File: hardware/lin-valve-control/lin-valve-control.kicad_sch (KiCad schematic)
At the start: 27 parts, among them J1 QWIIC Connector, J2 DIN-5_180degree, J3 DIN-5_180degree, J4 Screw_Terminal_01x02, J5 Screw_Terminal_01x03, J6 Screw_Terminal_01x03, Q1 2N7002, Q2 2N7002, U1 Arduino_Nano_v3.x, U2 TJA1021T, U3 DRV8833PWP

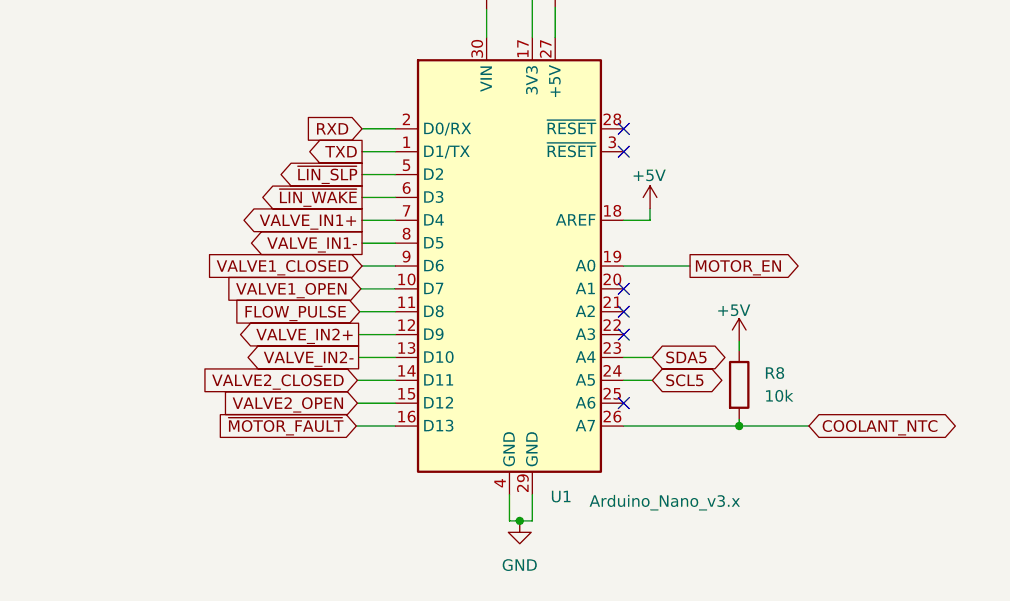
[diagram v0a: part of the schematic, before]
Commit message: Added firmware v1 for the valve-control board
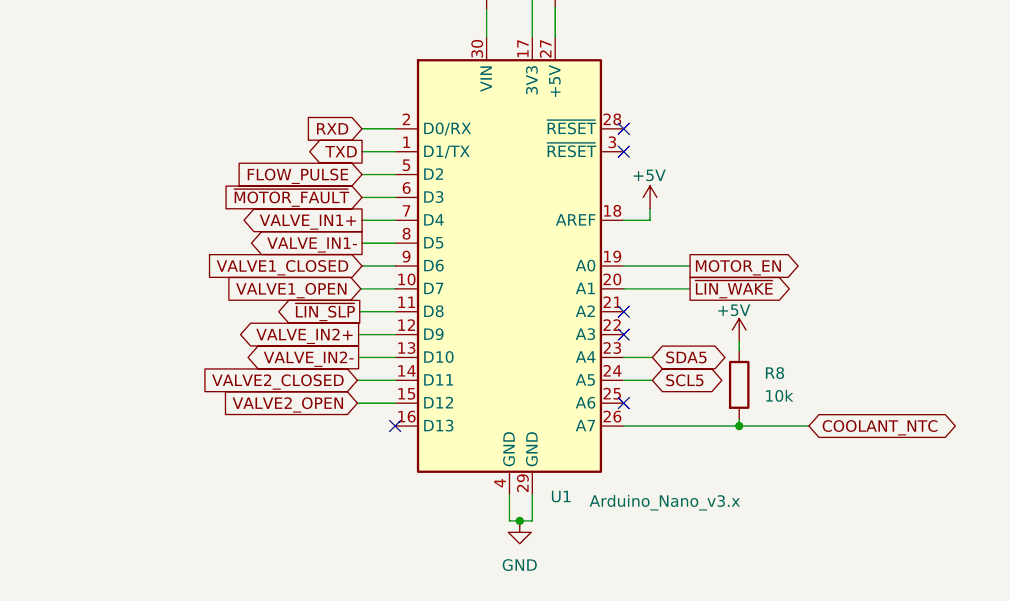
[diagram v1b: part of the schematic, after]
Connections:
- net FLOW_PULSE: now also U1.5 (D2); no longer U1.11 (D8)
- net ~{LIN_SLP}: now also U1.11 (D8); no longer U1.5 (D2)
- net ~{LIN_WAKE}: now also U1.20 (A1); no longer U1.6 (D3)
- net ~{MOTOR_FAULT}: now also U1.6 (D3); no longer U1.16 (D13)
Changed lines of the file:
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@@
   )
   (no_connect (at 63.754 170.561))
-  (no_connect (at 77.978 56.896))
   (no_connect (at 77.978 69.596))
   (no_connect (at 77.978 39.116))
   (no_connect (at 77.978 61.976))
+  (no_connect (at 52.578 72.136))
   (no_connect (at 77.978 41.656))
   (no_connect (at 77.978 59.436))
@@
     (stroke (width 0) (type default) (color 0 0 0 0))
   )
-  (wire (pts (xy 48.26 72.136) (xy 52.578 72.136))
-    (stroke (width 0) (type default) (color 0 0 0 0))
-  )
   (wire (pts (xy 42.164 105.41) (xy 42.164 107.569))
     (stroke (width 0) (type default) (color 0 0 0 0))
@@
   )
   (wire (pts (xy 187.96 38.1) (xy 197.485 38.1))
+    (stroke (width 0) (type default) (color 0 0 0 0))
+  )
+  (wire (pts (xy 77.978 56.896) (xy 85.344 56.896))
     (stroke (width 0) (type default) (color 0 0 0 0))
   )
@@
     )
   )
-  (global_label "~{LIN_WAKE}" (shape output) (at 48.895 46.736 180) (fields_autoplaced)
-    (effects (font (size 1.27 1.27)) (justify right))
-    (property "Intersheet References" "${INTERSHEET_REFS}" (id 0) (at 37.6808 46.6566 0)
-      (effects (font (size 1.27 1.27)) (justify right) hide)
+  (global_label "~{LIN_WAKE}" (shape output) (at 85.344 56.896 0) (fields_autoplaced)
+    (effects (font (size 1.27 1.27)) (justify left))
+    (property "Intersheet References" "${INTERSHEET_REFS}" (id 0) (at 96.5582 56.8166 0)
+      (effects (font (size 1.27 1.27)) (justify left) hide)
     )
   )
@@
     )
   )
-  (global_label "~{LIN_SLP}" (shape output) (at 48.895 44.196 180) (fields_autoplaced)
-    (effects (font (size 1.27 1.27)) (justify right))
-    (property "Intersheet References" "${INTERSHEET_REFS}" (id 0) (at 39.1322 44.1166 0)
+  (global_label "~{LIN_SLP}" (shape output) (at 48.641 59.436 180) (fields_autoplaced)
+    (effects (font (size 1.27 1.27)) (justify right))
+    (property "Intersheet References" "${INTERSHEET_REFS}" (id 0) (at 38.8782 59.3566 0)
       (effects (font (size 1.27 1.27)) (justify right) hide)
     )
@@
     )
   )
-  (global_label "FLOW_PULSE" (shape input) (at 48.641 59.436 180) (fields_autoplaced)
-    (effects (font (size 1.27 1.27)) (justify right))
-    (property "Intersheet References" "${INTERSHEET_REFS}" (id 0) (at 34.4635 59.3566 0)
+  (global_label "FLOW_PULSE" (shape input) (at 48.895 44.196 180) (fields_autoplaced)
+    (effects (font (size 1.27 1.27)) (justify right))
+    (property "Intersheet References" "${INTERSHEET_REFS}" (id 0) (at 34.7175 44.1166 0)
       (effects (font (size 1.27 1.27)) (justify right) hide)
     )
@@
     )
   )
-  (global_label "~{MOTOR_FAULT}" (shape input) (at 48.26 72.136 180) (fields_autoplaced)
-    (effects (font (size 1.27 1.27)) (justify right))
-    (property "Intersheet References" "${INTERSHEET_REFS}" (id 0) (at 33.1148 72.0566 0)
+  (global_label "~{MOTOR_FAULT}" (shape input) (at 48.895 46.736 180) (fields_autoplaced)
+    (effects (font (size 1.27 1.27)) (justify right))
+    (property "Intersheet References" "${INTERSHEET_REFS}" (id 0) (at 33.7498 46.6566 0)
       (effects (font (size 1.27 1.27)) (justify right) hide)
     )
@@
   (symbol (lib_id "power:+5V") (at 304.165 152.019 0) (unit 1)
     (in_bom yes) (on_board yes) (fields_autoplaced)
-    (property "Reference" "#PWR?" (id 0) (at 304.165 155.829 0)
+    (property "Reference" "#PWR0101" (id 0) (at 304.165 155.829 0)
       (effects (font (size 1.27 1.27)) hide)
     )
@@
     )
     (path "/fc94f245-2b8d-436c-b091-f7150042f6eb"
-      (reference "#PWR?") (unit 1) (value "+5V") (footprint "")
+      (reference "#PWR0101") (unit 1) (value "+5V") (footprint "")
     )
     (path "/c0e53e62-f89d-41ff-91b0-9eb5efa0a511"

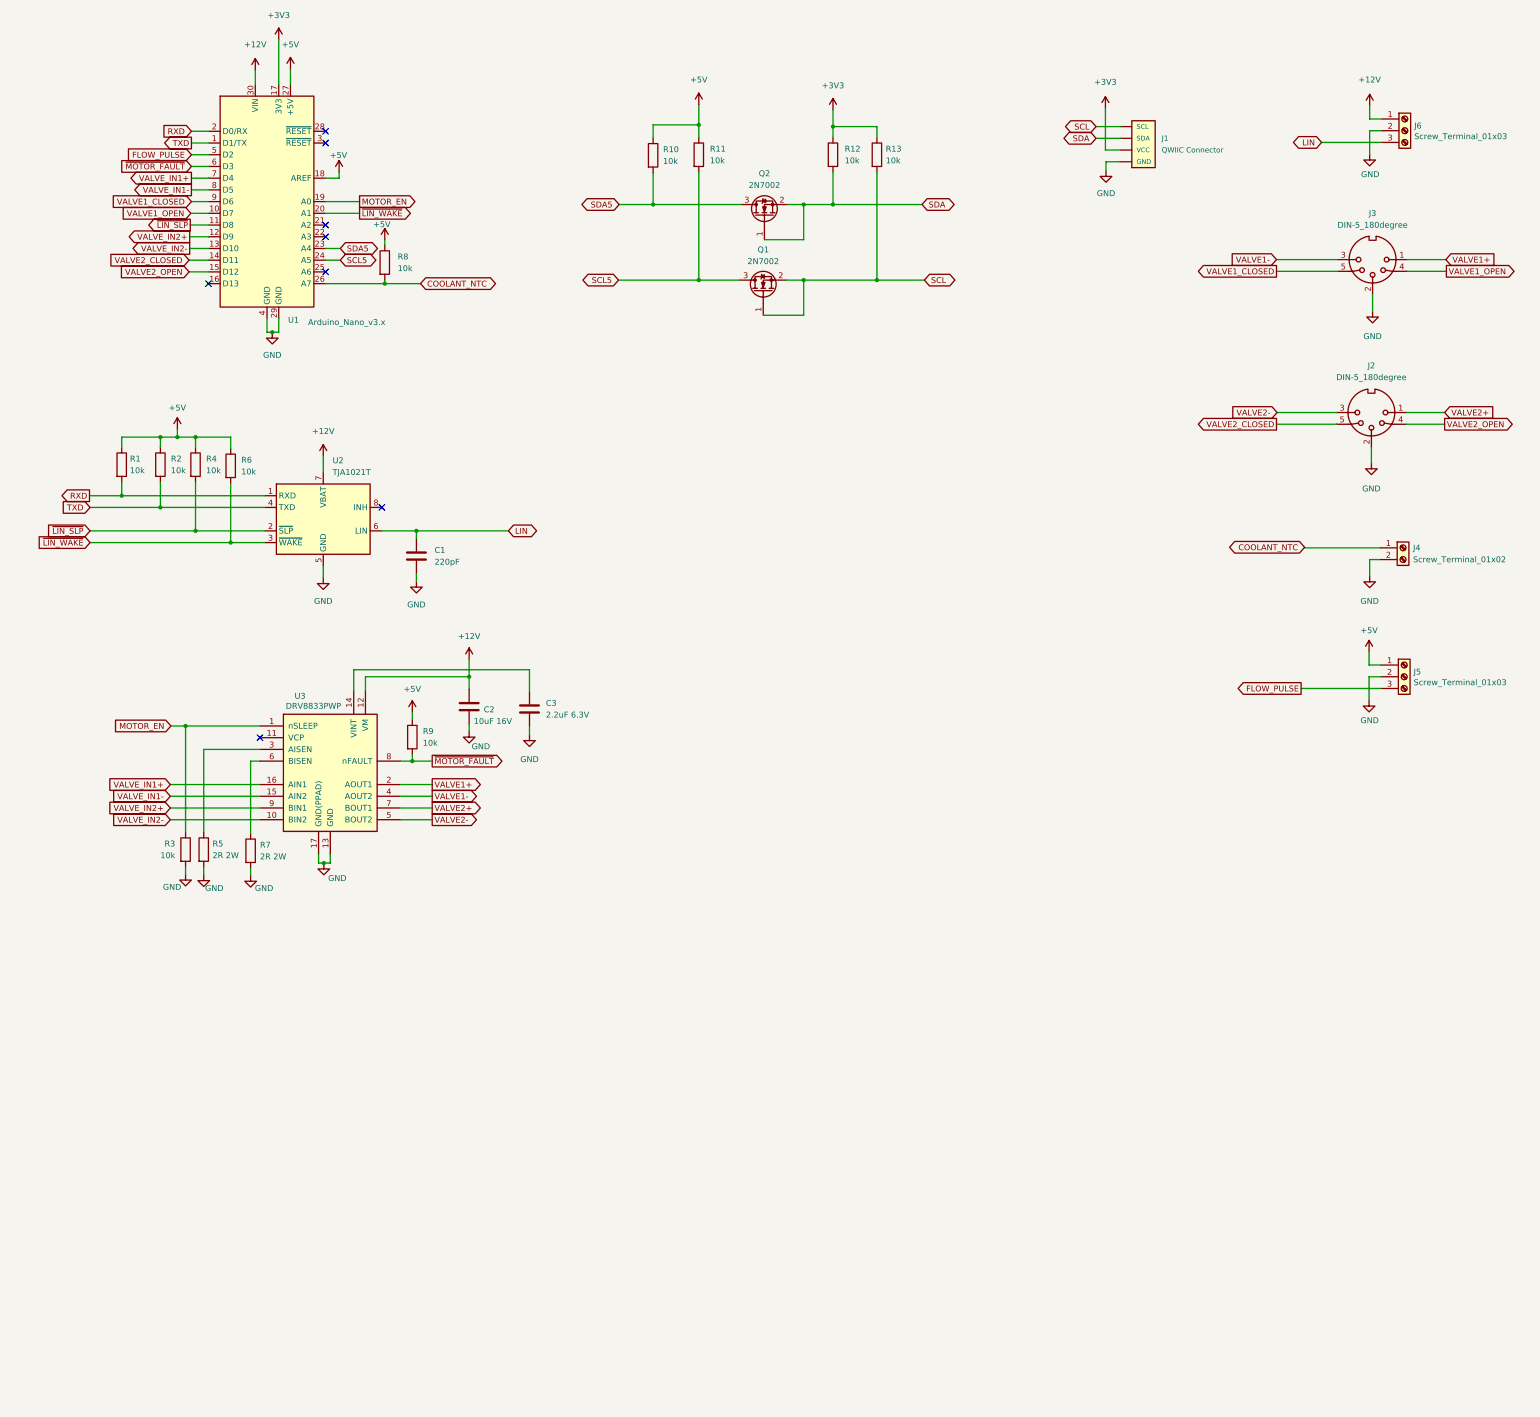
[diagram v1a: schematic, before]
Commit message: Added pins to control the cooling fan and the cooling pump
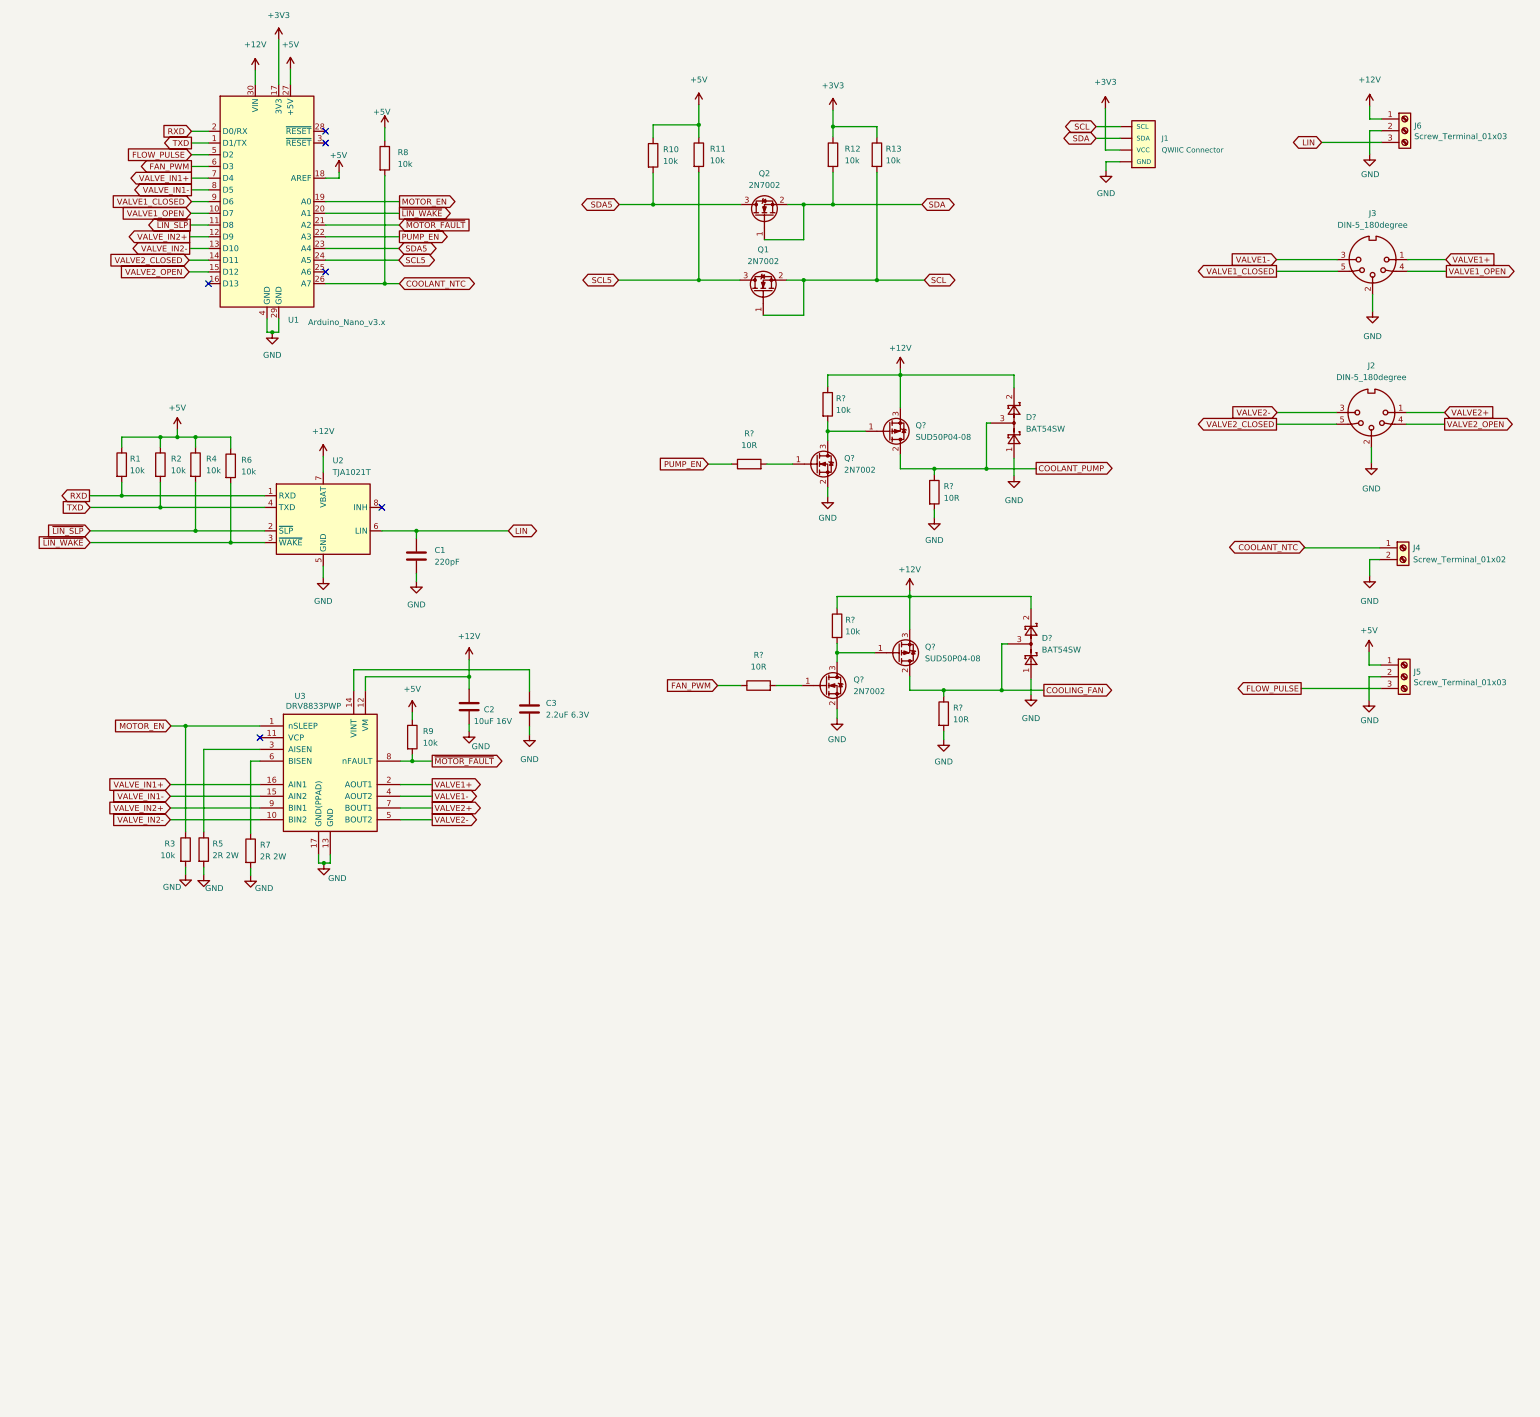
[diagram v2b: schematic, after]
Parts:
- added D? (x2): BAT54SW, Package_TO_SOT_SMD:SOT-323_SC-70, symbol Diode:BAT54SW
- added Q? (x2): 2N7002, Package_TO_SOT_SMD:SOT-23, symbol Transistor_FET:2N7002
- added Q? (x2): SUD50P04-08, Package_TO_SOT_SMD:TO-252-2, symbol Transistor_FET:SUD50P04-08
- added R? (x2): 10k, Resistor_SMD:R_0805_2012Metric_Pad1.20x1.40mm_HandSolder, symbol Device:R
- added R? (x4): 10R, Resistor_SMD:R_0805_2012Metric_Pad1.20x1.40mm_HandSolder, symbol Device:R
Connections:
- net +12V: now also D?.2, D?.2, Q?.3 (S), Q?.3 (S), R?.1, R?.1
- net GND: now also D?.1, D?.1, Q?.2 (S), Q?.2 (S), R?.2, R?.2
- net ~{MOTOR_FAULT}: now also U1.21 (A2); no longer U1.6 (D3)
- net PUMP_EN: now reaches U1.22 (A3)
- net PUMP_EN: now also R?.1
- new net: Q?.1 (G), R?.2 (x2)
- new net: Q?.1 (G), Q?.3 (D), R?.2 (x2)
- new net COOLANT_PUMP: D?.3, Q?.2 (D), R?.1
- new net COOLING_FAN: D?.3, Q?.2 (D), R?.1
- new net FAN_PWM: R?.1, U1.6 (D3)
- no-connect marks 8 -> 6
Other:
- moved on the sheet: R8

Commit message: Put in the Coolant Pump and Cooling Fan bits
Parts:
- added J?: Screw_Terminal_01x04, symbol Connector:Screw_Terminal_01x04
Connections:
- net COOLANT_PUMP: now also J?.1 (Pin_1)
- net COOLING_FAN: now also J?.3 (Pin_3)
- net GND: now also J?.2 (Pin_2), J?.4 (Pin_4)
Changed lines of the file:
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@@
   (junction (at 188.849 152.146) (diameter 0) (color 0 0 0 0)
+  )
+  (junction (at 250.571 136.398) (diameter 0) (color 0 0 0 0)
   )
   (junction (at 186.817 104.14) (diameter 0) (color 0 0 0 0)
@@
     (stroke (width 0) (type default) (color 0 0 0 0))
   )
+  (wire (pts (xy 253.238 131.318) (xy 250.571 131.318))
+    (stroke (width 0) (type default) (color 0 0 0 0))
+  )
   (wire (pts (xy 48.641 59.436) (xy 52.578 59.436))
     (stroke (width 0) (type default) (color 0 0 0 0))
@@
     (stroke (width 0) (type default) (color 0 0 0 0))
   )
+  (wire (pts (xy 250.571 136.398) (xy 253.238 136.398))
+    (stroke (width 0) (type default) (color 0 0 0 0))
+  )
   (wire (pts (xy 181.61 54.991) (xy 187.96 54.991))
     (stroke (width 0) (type default) (color 0 0 0 0))
@@
     (stroke (width 0) (type default) (color 0 0 0 0))
   )
+  (wire (pts (xy 248.666 128.778) (xy 253.238 128.778))
+    (stroke (width 0) (type default) (color 0 0 0 0))
+  )
   (wire (pts (xy 209.931 112.268) (xy 209.931 113.538))
     (stroke (width 0) (type default) (color 0 0 0 0))
@@
     (stroke (width 0) (type default) (color 0 0 0 0))
   )
+  (wire (pts (xy 250.571 141.732) (xy 250.571 136.398))
+    (stroke (width 0) (type default) (color 0 0 0 0))
+  )
   (wire (pts (xy 204.597 139.954) (xy 204.597 147.066))
     (stroke (width 0) (type default) (color 0 0 0 0))
   )
+  (wire (pts (xy 248.285 133.858) (xy 253.238 133.858))
+    (stroke (width 0) (type default) (color 0 0 0 0))
+  )
   (wire (pts (xy 94.234 185.801) (xy 101.092 185.801))
     (stroke (width 0) (type default) (color 0 0 0 0))
   )
   (wire (pts (xy 48.895 44.196) (xy 52.578 44.196))
+    (stroke (width 0) (type default) (color 0 0 0 0))
+  )
+  (wire (pts (xy 250.571 131.318) (xy 250.571 136.398))
     (stroke (width 0) (type default) (color 0 0 0 0))
   )
@@
     )
   )
+  (global_label "COOLANT_PUMP" (shape input) (at 248.666 128.778 180) (fields_autoplaced)
+    (effects (font (size 1.27 1.27)) (justify right))
+    (property "Intersheet References" "${INTERSHEET_REFS}" (id 0) (at 231.7066 128.6986 0)
+      (effects (font (size 1.27 1.27)) (justify right) hide)
+    )
+  )
   (global_label "LIN" (shape bidirectional) (at 293.878 41.529 180) (fields_autoplaced)
     (effects (font (size 1.27 1.27)) (justify right))
@@
     (property "Intersheet References" "${INTERSHEET_REFS}" (id 0) (at 109.1856 72.0566 0)
       (effects (font (size 1.27 1.27)) (justify left) hide)
+    )
+  )
+  (global_label "COOLING_FAN" (shape input) (at 248.285 133.858 180) (fields_autoplaced)
+    (effects (font (size 1.27 1.27)) (justify right))
+    (property "Intersheet References" "${INTERSHEET_REFS}" (id 0) (at 233.3213 133.7786 0)
+      (effects (font (size 1.27 1.27)) (justify right) hide)
     )
   )
@@
     (pin "3")
     (pin "4")
+  )
+  (symbol (lib_id "power:GND") (at 250.571 141.732 0) (unit 1)
+    (in_bom yes) (on_board yes) (fields_autoplaced)
+    (property "Reference" "#PWR?" (id 0) (at 250.571 148.082 0)
+      (effects (font (size 1.27 1.27)) hide)
+    )
+    (property "Value" "GND" (id 1) (at 250.571 146.939 0))
+    (property "Footprint" "" (id 2) (at 250.571 141.732 0)
+      (effects (font (size 1.27 1.27)) hide)
+    )
+    (property "Datasheet" "" (id 3) (at 250.571 141.732 0)
+      (effects (font (size 1.27 1.27)) hide)
+    )
+    (pin "1")
   )
   (symbol (lib_id "power:+5V") (at 90.805 38.354 0) (unit 1)
@@
     (pin "2")
     (pin "3")
+  )
+  (symbol (lib_id "Connector:Screw_Terminal_01x04") (at 258.318 131.318 0) (unit 1)
+    (in_bom yes) (on_board yes) (fields_autoplaced)
+    (property "Reference" "J?" (id 0) (at 261.493 131.3179 0)
+      (effects (font (size 1.27 1.27)) (justify left))
+    )
+    (property "Value" "Screw_Terminal_01x04" (id 1) (at 261.493 133.8579 0)
+      (effects (font (size 1.27 1.27)) (justify left))
+    )
+    (property "Footprint" "" (id 2) (at 258.318 131.318 0)
+      (effects (font (size 1.27 1.27)) hide)
+    )
+    (property "Datasheet" "~" (id 3) (at 258.318 131.318 0)
+      (effects (font (size 1.27 1.27)) hide)
+    )
+    (pin "1")
+    (pin "2")
+    (pin "3")
+    (pin "4")
   )
   (symbol (lib_name "GND_2") (lib_id "power:GND") (at 188.849 166.37 0) (unit 1)
@@
       (reference "#PWR?") (unit 1) (value "GND") (footprint "")
     )
+    (path "/5e3856f0-4f55-4eb2-9a3b-820f2ed2f81a"
+      (reference "#PWR?") (unit 1) (value "GND") (footprint "")
+    )
     (path "/6a773d6f-a6af-4b0a-a939-9c80148855e4"
       (reference "#PWR?") (unit 1) (value "GND") (footprint "")
@@
       (reference "J6") (unit 1) (value "Screw_Terminal_01x03") (footprint "TerminalBlock_TE-Connectivity:TerminalBlock_TE_282834-3_1x03_P2.54mm_Horizontal")
     )
+    (path "/95ef4bb8-f5c1-4c5e-817b-ad10fe2c586a"
+      (reference "J?") (unit 1) (value "Screw_Terminal_01x04") (footprint "TerminalBlock_TE-Connectivity:TerminalBlock_TE_282834-4_1x04_P2.54mm_Horizontal")
+    )
     (path "/795389c3-af13-4fd1-9c9c-4dc74b83a7bf"

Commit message: Sigh.  forgot to save.
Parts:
- gave numbers to parts that had none: 13
- renumbered J2 to J3, J3 to J4, J4 to J5, J5 to J6, J6 to J7, R12 to R15, R13 to R17
